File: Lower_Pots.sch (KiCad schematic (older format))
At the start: 17 parts, among them U5 CD74HC4067M

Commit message: Sub boards completed
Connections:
- net Mult_1 renamed S0
- net Mult_2 renamed S1
- net Mult_3 renamed S2
- net Mult_4 renamed S3
- net POTS_2 renamed LOWER_POTS
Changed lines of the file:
@@
 Connection ~ 2700 7100
 Text HLabel 1650 1900 0    50   Input ~ 0
-POTS_2
+LOWER_POTS
 Wire Wire Line
 	1650 1900 2200 1900
-Text GLabel 2000 2600 0    50   Input ~ 0
-Mult_4
 Wire Wire Line
 	2000 2600 2200 2600
-Text GLabel 2000 2300 0    50   Input ~ 0
-Mult_1
-Text GLabel 2000 2400 0    50   Input ~ 0
-Mult_2
-Text GLabel 2000 2500 0    50   Input ~ 0
-Mult_3
 Wire Wire Line
 	2000 2300 2200 2300
@@
 Wire Wire Line
 	4800 1150 4800 1400
+Text GLabel 2000 2300 0    50   Input ~ 0
+S0
+Text GLabel 2000 2400 0    50   Input ~ 0
+S1
+Text GLabel 2000 2500 0    50   Input ~ 0
+S2
+Text GLabel 2000 2600 0    50   Input ~ 0
+S3
 $EndSCHEMATC

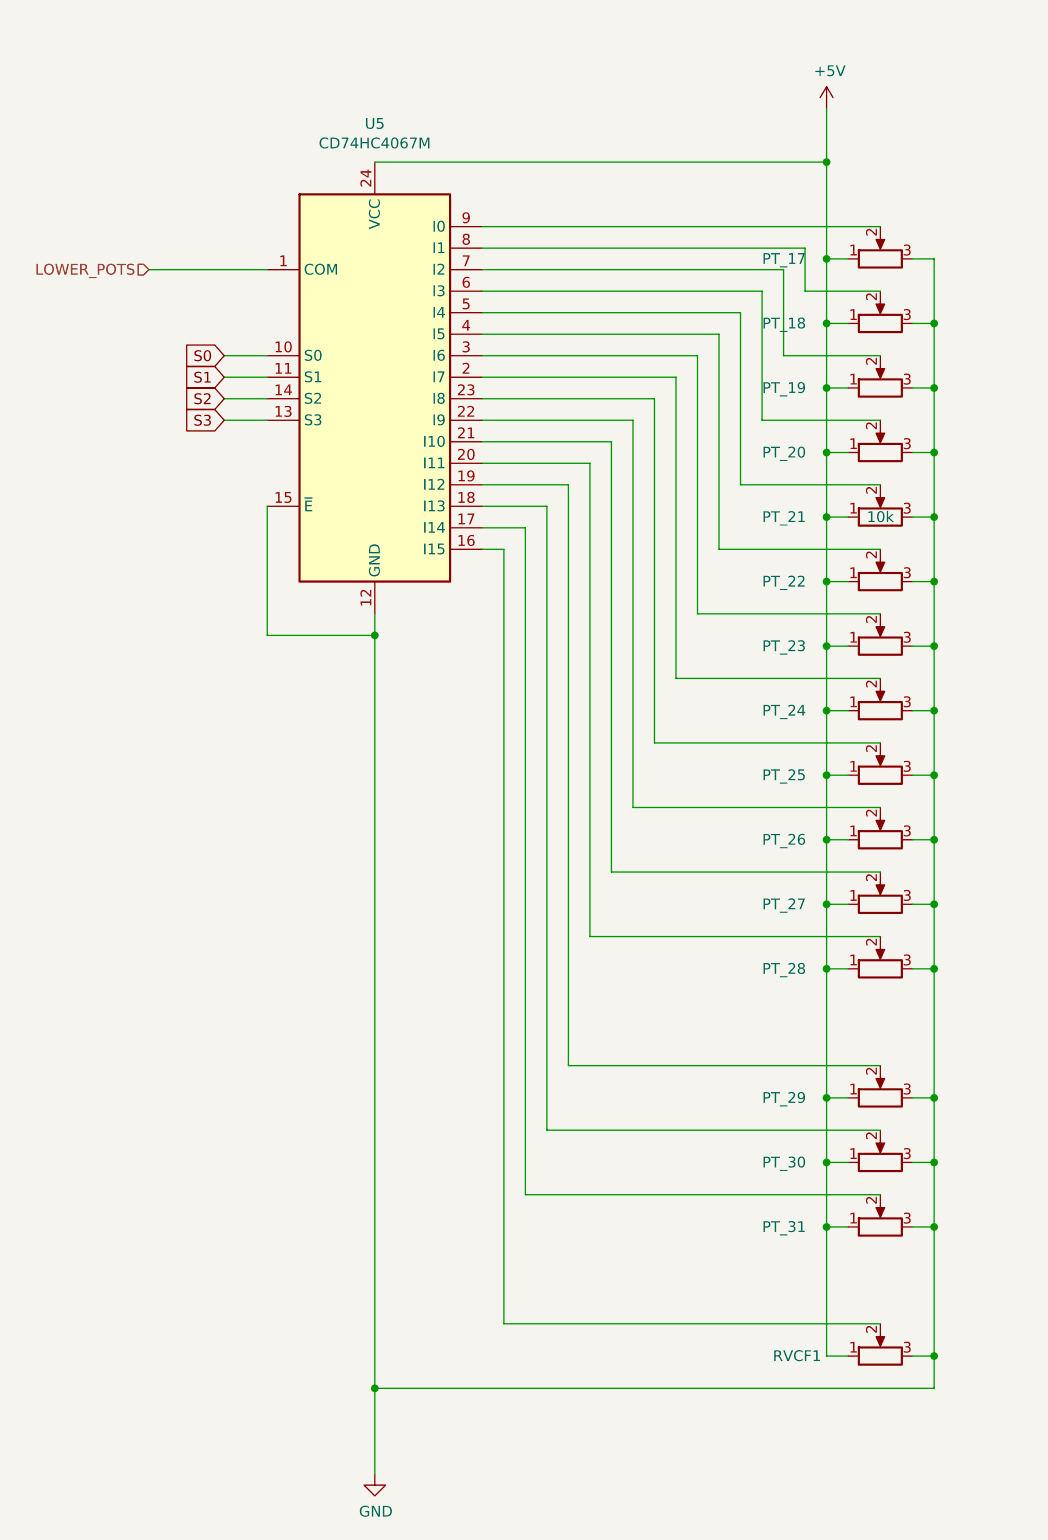
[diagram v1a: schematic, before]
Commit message: Tidy schematic / renumber components / complete daughter boards
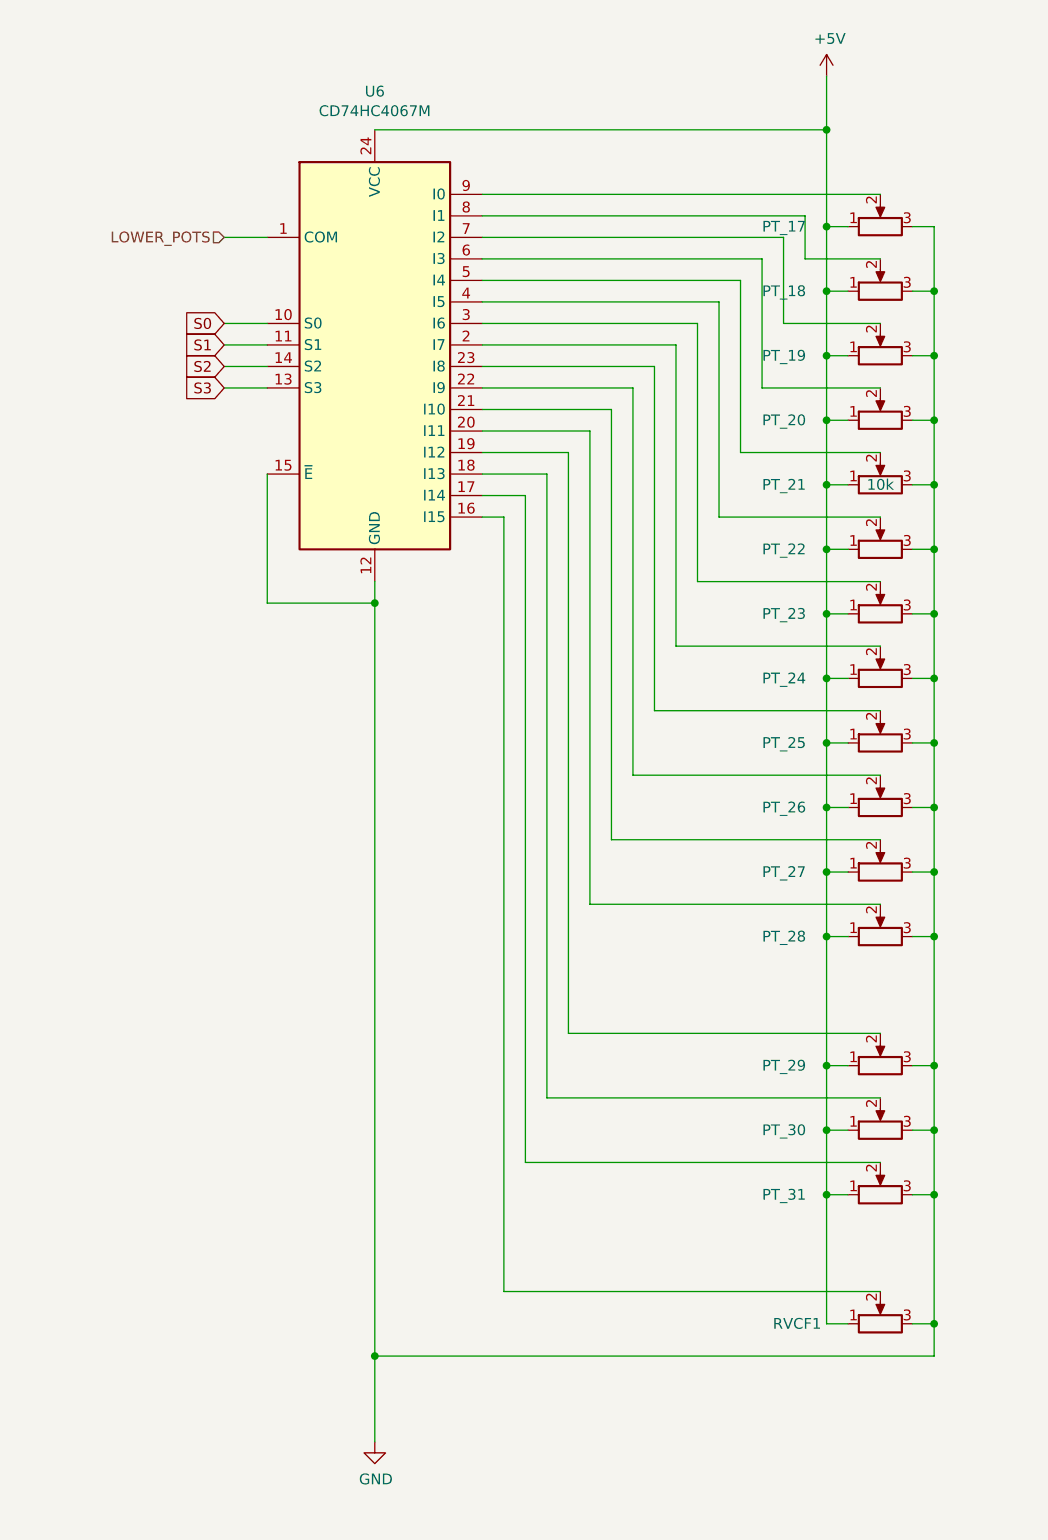
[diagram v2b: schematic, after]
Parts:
- RVCF1: value R_POT -> PTA4543
- renumbered U5 to U6
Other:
- moved on the sheet: PT_17, PT_18, PT_19, PT_20, PT_21, PT_22, PT_23, PT_24, PT_25, PT_26, PT_27, PT_28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

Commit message: Moved connection to crossfader to ease pin assignment on multiplexer
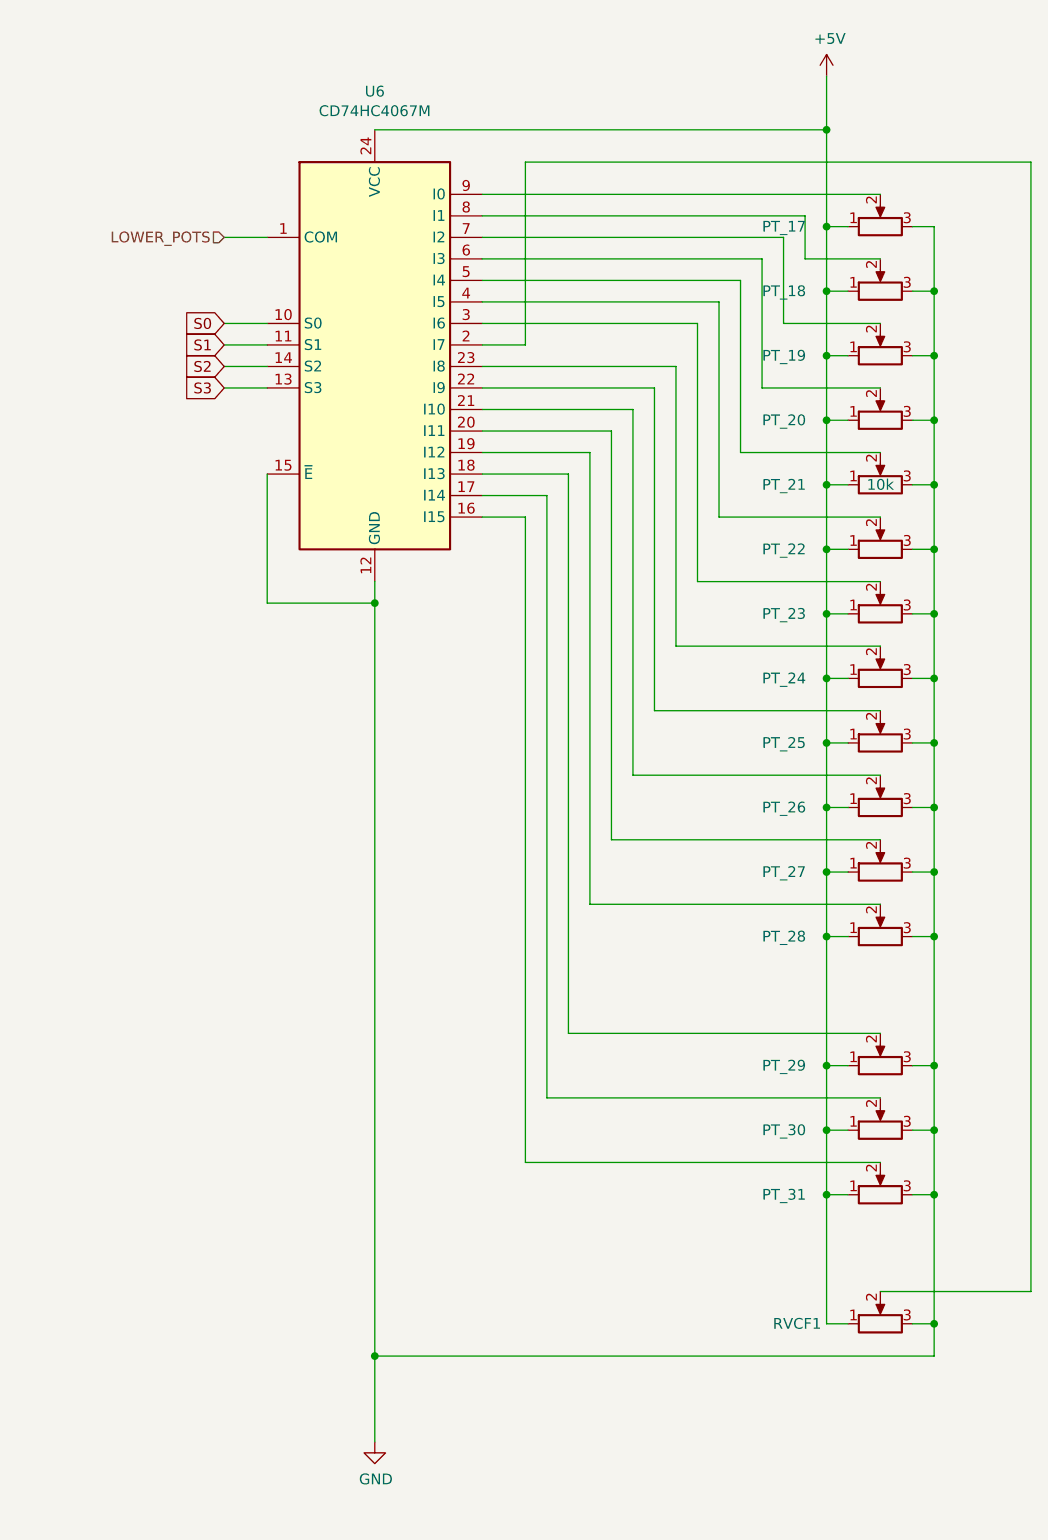
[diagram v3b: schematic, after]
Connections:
- net at PT_24.2: now also U6.23 (I8); no longer U6.2 (I7)
- net at PT_25.2: now also U6.22 (I9); no longer U6.23 (I8)
- net at PT_26.2: now also U6.21 (I10); no longer U6.22 (I9)
- net at PT_27.2: now also U6.20 (I11); no longer U6.21 (I10)
- net at PT_28.2: now also U6.19 (I12); no longer U6.20 (I11)
- net at RVCF1.2: now also U6.2 (I7); no longer U6.16 (I15)
- net at PT_29.2: now also U6.18 (I13); no longer U6.19 (I12)
- net at PT_30.2: now also U6.17 (I14); no longer U6.18 (I13)
- net at PT_31.2: now also U6.16 (I15); no longer U6.17 (I14)
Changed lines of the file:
@@
 	4700 1850 5050 1850
 Wire Wire Line
-	4100 3650 4100 2250
+	4100 3650 4100 2350
 Connection ~ 4800 3200
 Connection ~ 5300 3200
@@
 	3200 1950 4400 1950
 Wire Wire Line
-	3200 2650 3700 2650
-Wire Wire Line
-	3200 2550 3800 2550
-Wire Wire Line
-	3200 2450 3900 2450
-Wire Wire Line
-	3200 2350 4000 2350
-Wire Wire Line
-	4000 2350 4000 3950
-Wire Wire Line
-	3200 2250 4100 2250
-Wire Wire Line
 	3200 2150 4200 2150
 Wire Wire Line
 	3200 2050 4300 2050
-Wire Wire Line
-	3700 2650 3700 4850
-Wire Wire Line
-	3800 2550 3800 4550
-Wire Wire Line
-	3900 2450 3900 4250
 Wire Wire Line
 	5050 1550 3200 1550
@@
 Connection ~ 4800 6200
 Wire Wire Line
-	3200 2750 3600 2750
-Wire Wire Line
-	3600 2750 3600 5450
-Wire Wire Line
 	3600 5450 5050 5450
 Wire Wire Line
-	3200 2850 3500 2850
-Wire Wire Line
-	3500 2850 3500 5750
-Wire Wire Line
 	3500 5750 5050 5750
 Wire Wire Line
-	3400 2950 3400 6050
-Wire Wire Line
 	3400 6050 5050 6050
-Wire Wire Line
-	3200 3050 3300 3050
-Wire Wire Line
-	3300 3050 3300 6650
-Wire Wire Line
-	3300 6650 5050 6650
-Wire Wire Line
-	3200 2950 3400 2950
 Wire Wire Line
 	2700 3350 2700 3450
@@
 Wire Wire Line
 	2000 1750 2200 1750
+Wire Wire Line
+	3400 3050 3200 3050
+Wire Wire Line
+	3400 3050 3400 6050
+Wire Wire Line
+	3500 2950 3200 2950
+Wire Wire Line
+	3500 2950 3500 5750
+Wire Wire Line
+	3600 2850 3200 2850
+Wire Wire Line
+	3600 2850 3600 5450
+Wire Wire Line
+	3700 2750 3200 2750
+Wire Wire Line
+	3700 2750 3700 4850
+Wire Wire Line
+	3800 2650 3200 2650
+Wire Wire Line
+	3800 2650 3800 4550
+Wire Wire Line
+	3900 2550 3200 2550
+Wire Wire Line
+	3900 2550 3900 4250
+Wire Wire Line
+	4000 2450 3200 2450
+Wire Wire Line
+	4000 2450 4000 3950
+Wire Wire Line
+	4100 2350 3200 2350
+Wire Wire Line
+	3200 2250 3400 2250
+Wire Wire Line
+	3400 2250 3400 1400
+Wire Wire Line
+	3400 1400 5750 1400
+Wire Wire Line
+	5750 1400 5750 6650
+Wire Wire Line
+	5750 6650 5050 6650
 $EndSCHEMATC

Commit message: Redesign of upper boards
Added bussed resistors following Igor's correction to the schematic + tidied schematic.
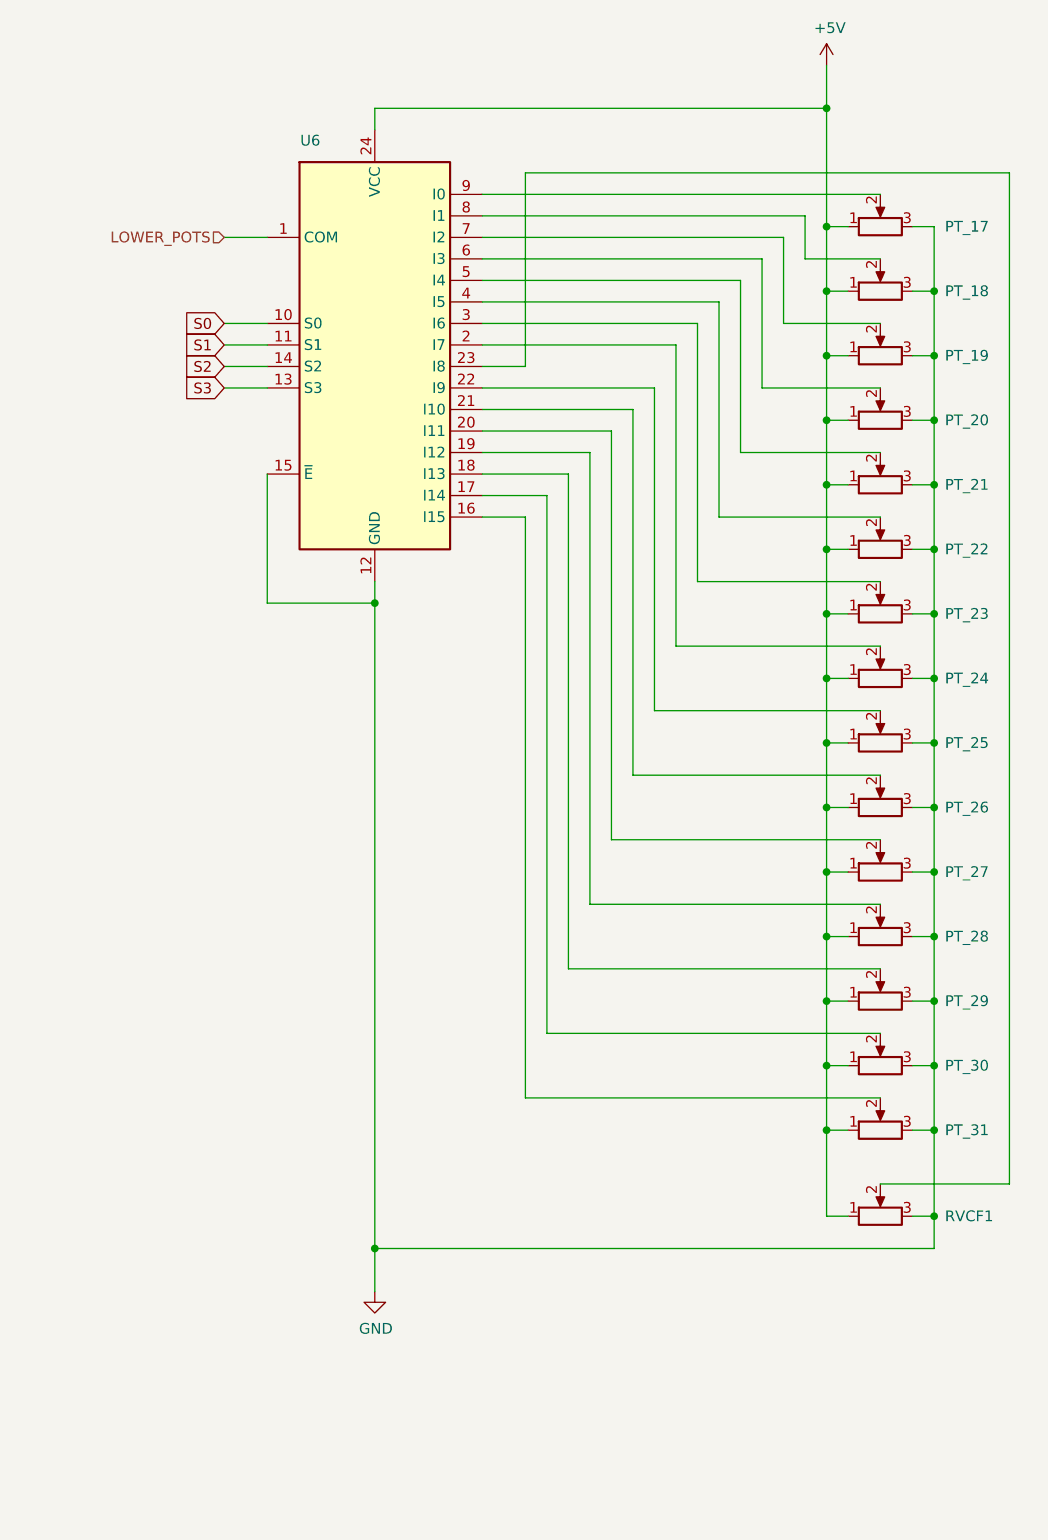
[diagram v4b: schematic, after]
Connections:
- net at PT_24.2: now also U6.2 (I7); no longer U6.23 (I8)
- net at RVCF1.2: now also U6.23 (I8); no longer U6.2 (I7)
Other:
- moved on the sheet: PT_29, PT_30, PT_31, RVCF1
